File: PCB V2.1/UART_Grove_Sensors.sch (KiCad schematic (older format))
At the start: 11 parts, among them J5 B4B-PH-K-S(LF)(SN), J6 B4B-PH-K-S(LF)(SN), J7 B4B-PH-K-S(LF)(SN), J8 B4B-PH-K-S(LF)(SN), U4 74HC4052D

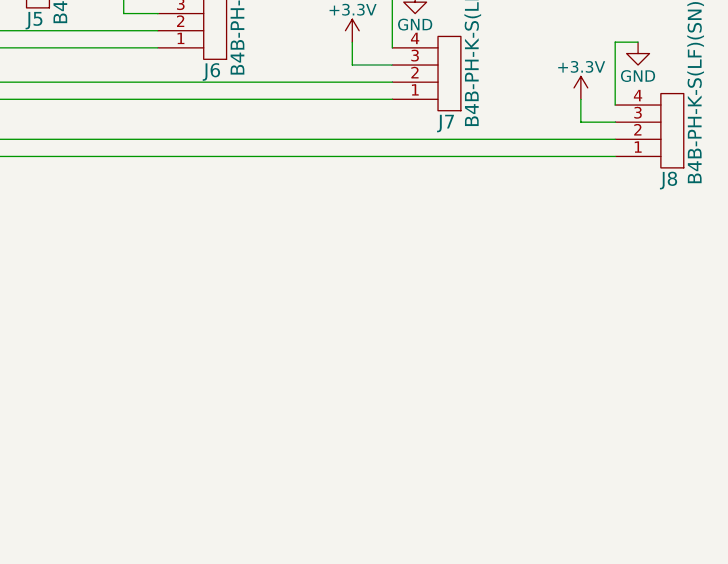
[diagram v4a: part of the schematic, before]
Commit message: Revert "Placement near completeq"
This reverts commit ae7bce2a0b52adb9ec10d03d9117548a28df5835.
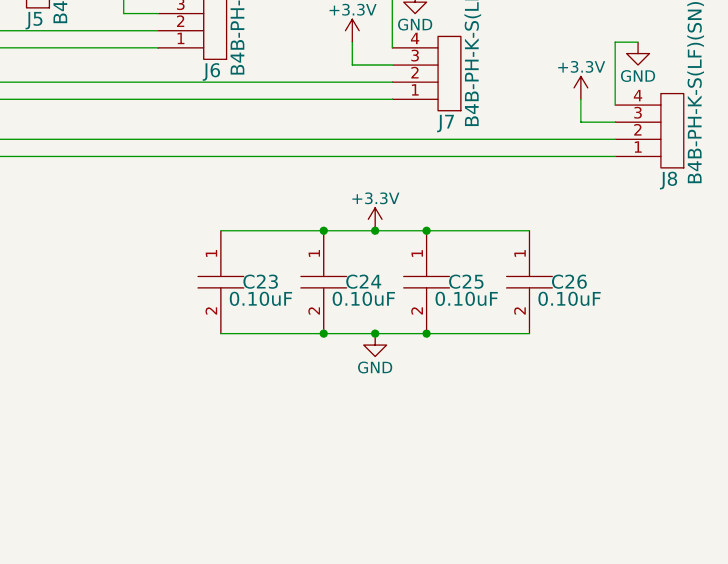
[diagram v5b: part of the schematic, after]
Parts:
- added C23, C24, C25, C26: CL05B104JP5NNNC, PCB_Footprints:C0402, symbol CL05B104JP5NNNC
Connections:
- net +3V3: now also C23.1, C24.1, C25.1, C26.1
- net GND: now also C23.2, C24.2, C25.2, C26.2
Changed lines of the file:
@@
+$EndComp
+$Comp
+L CL05B104JP5NNNC C23
+U 1 1 57D8F945
+P 7925 5275
+F 0 "C23" V 7900 5450 60  0000 C CNN
+F 1 "CL05B104JP5NNNC" H 7975 5125 60  0001 C CNN
+F 2 "PCB_Footprints:C0402" H 8175 5325 60  0001 C CNN
+F 3 "http://www.samsungsem.com/kr/support/product-search/mlcc/__icsFiles/afieldfile/2016/08/18/S_CL05B104JP5NNNC.pdf" H 8175 5325 60  0001 C CNN
+F 4 "$0.00903 @ 5000" H 7825 5525 60  0001 C CNN "Cost"
+F 5 "4 Sept 2016" H 7925 5625 60  0001 C CNN "Date Created"
+F 6 "5 Sept 2016" H 8025 5725 60  0001 C CNN "Date Modified"
+F 7 "Adam Vadala-Roth" H 8125 5825 60  0001 C CNN "Designer"
+F 8 "0.55mm" H 8225 5925 60  0001 C CNN "Height"
+F 9 "Yes" H 8325 6025 60  0001 C CNN "RHoS?"
+F 10 "Samsung Electro-Mechanics America, Inc." H 8425 6125 60  0001 C CNN "MFR"
+F 11 "CL05B104JP5NNNC" H 8525 6225 60  0001 C CNN "MFR#"
+F 12 "SMT/SMD" H 8625 6325 60  0001 C CNN "Mounting"
+F 13 "2" H 8725 6425 60  0001 C CNN "Pint Count#"
+F 14 "Active" H 8825 6525 60  0001 C CNN "Status"
+F 15 "5%" H 8925 6625 60  0001 C CNN "Tolerance"
+F 16 "Ceramic Capacitor 0402" H 9025 6725 60  0001 C CNN "Type"
+F 17 "10V" H 9125 6825 60  0001 C CNN "Voltage"
+F 18 "N/A" H 9225 6925 60  0001 C CNN "Wattage"
+F 19 "0.10uF" V 7975 5450 60  0000 C CNN "Component-Value"
+F 20 "0.10µF 10V Ceramic Capacitor X7R 0402 (1005 Metric) 0.039\" L x 0.020\" W (1.00mm x 0.50mm)" H 9425 7125 60  0001 C CNN "Description"
+	1    7925 5275
+	0    1    1    0
 $EndComp
 $Comp
@@
 $EndComp
 $Comp
+L GND #PWR51
+U 1 1 57D95A00
+P 8600 5475
+F 0 "#PWR51" H 8600 5225 50  0001 C CNN
+F 1 "GND" H 8600 5325 50  0000 C CNN
+F 2 "" H 8600 5475 50  0000 C CNN
+F 3 "" H 8600 5475 50  0000 C CNN
+	1    8600 5475
+	1    0    0    -1
+$EndComp
+$Comp
 L GND #PWR52
 U 1 1 57D95B46
@@
 F 3 "" H 8775 3975 50  0000 C CNN
 	1    8775 3975
+	1    0    0    -1
+$EndComp
+$Comp
+L CL05B104JP5NNNC C24
+U 1 1 57D961FE
+P 8375 5275
+F 0 "C24" V 8350 5450 60  0000 C CNN
+F 1 "CL05B104JP5NNNC" H 8425 5125 60  0001 C CNN
+F 2 "PCB_Footprints:C0402" H 8625 5325 60  0001 C CNN
+F 3 "http://www.samsungsem.com/kr/support/product-search/mlcc/__icsFiles/afieldfile/2016/08/18/S_CL05B104JP5NNNC.pdf" H 8625 5325 60  0001 C CNN
+F 4 "$0.00903 @ 5000" H 8275 5525 60  0001 C CNN "Cost"
+F 5 "4 Sept 2016" H 8375 5625 60  0001 C CNN "Date Created"
+F 6 "5 Sept 2016" H 8475 5725 60  0001 C CNN "Date Modified"
+F 7 "Adam Vadala-Roth" H 8575 5825 60  0001 C CNN "Designer"
+F 8 "0.55mm" H 8675 5925 60  0001 C CNN "Height"
+F 9 "Yes" H 8775 6025 60  0001 C CNN "RHoS?"
+F 10 "Samsung Electro-Mechanics America, Inc." H 8875 6125 60  0001 C CNN "MFR"
+F 11 "CL05B104JP5NNNC" H 8975 6225 60  0001 C CNN "MFR#"
+F 12 "SMT/SMD" H 9075 6325 60  0001 C CNN "Mounting"
+F 13 "2" H 9175 6425 60  0001 C CNN "Pint Count#"
+F 14 "Active" H 9275 6525 60  0001 C CNN "Status"
+F 15 "5%" H 9375 6625 60  0001 C CNN "Tolerance"
+F 16 "Ceramic Capacitor 0402" H 9475 6725 60  0001 C CNN "Type"
+F 17 "10V" H 9575 6825 60  0001 C CNN "Voltage"
+F 18 "N/A" H 9675 6925 60  0001 C CNN "Wattage"
+F 19 "0.10uF" V 8425 5450 60  0000 C CNN "Component-Value"
+F 20 "0.10µF 10V Ceramic Capacitor X7R 0402 (1005 Metric) 0.039\" L x 0.020\" W (1.00mm x 0.50mm)" H 9875 7125 60  0001 C CNN "Description"
+	1    8375 5275
+	0    1    1    0
+$EndComp
+$Comp
+L CL05B104JP5NNNC C25
+U 1 1 57D9626E
+P 8825 5275
+F 0 "C25" V 8800 5450 60  0000 C CNN
+F 1 "CL05B104JP5NNNC" H 8875 5125 60  0001 C CNN
+F 2 "PCB_Footprints:C0402" H 9075 5325 60  0001 C CNN
+F 3 "http://www.samsungsem.com/kr/support/product-search/mlcc/__icsFiles/afieldfile/2016/08/18/S_CL05B104JP5NNNC.pdf" H 9075 5325 60  0001 C CNN
+F 4 "$0.00903 @ 5000" H 8725 5525 60  0001 C CNN "Cost"
+F 5 "4 Sept 2016" H 8825 5625 60  0001 C CNN "Date Created"
+F 6 "5 Sept 2016" H 8925 5725 60  0001 C CNN "Date Modified"
+F 7 "Adam Vadala-Roth" H 9025 5825 60  0001 C CNN "Designer"
+F 8 "0.55mm" H 9125 5925 60  0001 C CNN "Height"
+F 9 "Yes" H 9225 6025 60  0001 C CNN "RHoS?"
+F 10 "Samsung Electro-Mechanics America, Inc." H 9325 6125 60  0001 C CNN "MFR"
+F 11 "CL05B104JP5NNNC" H 9425 6225 60  0001 C CNN "MFR#"
+F 12 "SMT/SMD" H 9525 6325 60  0001 C CNN "Mounting"
+F 13 "2" H 9625 6425 60  0001 C CNN "Pint Count#"
+F 14 "Active" H 9725 6525 60  0001 C CNN "Status"
+F 15 "5%" H 9825 6625 60  0001 C CNN "Tolerance"
+F 16 "Ceramic Capacitor 0402" H 9925 6725 60  0001 C CNN "Type"
+F 17 "10V" H 10025 6825 60  0001 C CNN "Voltage"
+F 18 "N/A" H 10125 6925 60  0001 C CNN "Wattage"
+F 19 "0.10uF" V 8875 5450 60  0000 C CNN "Component-Value"
+F 20 "0.10µF 10V Ceramic Capacitor X7R 0402 (1005 Metric) 0.039\" L x 0.020\" W (1.00mm x 0.50mm)" H 10325 7125 60  0001 C CNN "Description"
+	1    8825 5275
+	0    1    1    0
+$EndComp
+$Comp
+L CL05B104JP5NNNC C26
+U 1 1 57D962E7
+P 9275 5275
+F 0 "C26" V 9250 5450 60  0000 C CNN
+F 1 "CL05B104JP5NNNC" H 9325 5125 60  0001 C CNN
+F 2 "PCB_Footprints:C0402" H 9525 5325 60  0001 C CNN
+F 3 "http://www.samsungsem.com/kr/support/product-search/mlcc/__icsFiles/afieldfile/2016/08/18/S_CL05B104JP5NNNC.pdf" H 9525 5325 60  0001 C CNN
+F 4 "$0.00903 @ 5000" H 9175 5525 60  0001 C CNN "Cost"
+F 5 "4 Sept 2016" H 9275 5625 60  0001 C CNN "Date Created"
+F 6 "5 Sept 2016" H 9375 5725 60  0001 C CNN "Date Modified"
+F 7 "Adam Vadala-Roth" H 9475 5825 60  0001 C CNN "Designer"
+F 8 "0.55mm" H 9575 5925 60  0001 C CNN "Height"
+F 9 "Yes" H 9675 6025 60  0001 C CNN "RHoS?"
+F 10 "Samsung Electro-Mechanics America, Inc." H 9775 6125 60  0001 C CNN "MFR"
+F 11 "CL05B104JP5NNNC" H 9875 6225 60  0001 C CNN "MFR#"
+F 12 "SMT/SMD" H 9975 6325 60  0001 C CNN "Mounting"
+F 13 "2" H 10075 6425 60  0001 C CNN "Pint Count#"
+F 14 "Active" H 10175 6525 60  0001 C CNN "Status"
+F 15 "5%" H 10275 6625 60  0001 C CNN "Tolerance"
+F 16 "Ceramic Capacitor 0402" H 10375 6725 60  0001 C CNN "Type"
+F 17 "10V" H 10475 6825 60  0001 C CNN "Voltage"
+F 18 "N/A" H 10575 6925 60  0001 C CNN "Wattage"
+F 19 "0.10uF" V 9325 5450 60  0000 C CNN "Component-Value"
+F 20 "0.10µF 10V Ceramic Capacitor X7R 0402 (1005 Metric) 0.039\" L x 0.020\" W (1.00mm x 0.50mm)" H 10775 7125 60  0001 C CNN "Description"
+	1    9275 5275
+	0    1    1    0
+$EndComp
+$Comp
+L +3.3V #PWR50
+U 1 1 57D9679F
+P 8600 5025
+F 0 "#PWR50" H 8600 4875 50  0001 C CNN
+F 1 "+3.3V" H 8600 5165 50  0000 C CNN
+F 2 "" H 8600 5025 50  0000 C CNN
+F 3 "" H 8600 5025 50  0000 C CNN
+	1    8600 5025
 	1    0    0    -1
 $EndComp
@@
 	6400 3850 6875 3850
 Wire Wire Line
+	7925 5475 9275 5475
+Wire Wire Line
+	7925 5025 9275 5025
+Connection ~ 8375 5475
+Connection ~ 8600 5475
+Connection ~ 8825 5475
+Connection ~ 8825 5025
+Connection ~ 8375 5025
+Connection ~ 8600 5025
+Wire Wire Line
 	4525 4700 4525 5400
